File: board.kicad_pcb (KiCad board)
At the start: 2 copper layers, 40 parts, among them J1 TEMPS, J2 OLED, J3 RELAY, J4 RELAY_EN, J5 PWR_IN, J6 CONN_PROG, Q1 BC847, Q2 BC847, SW1 SW_RST, SW2 SW_RST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

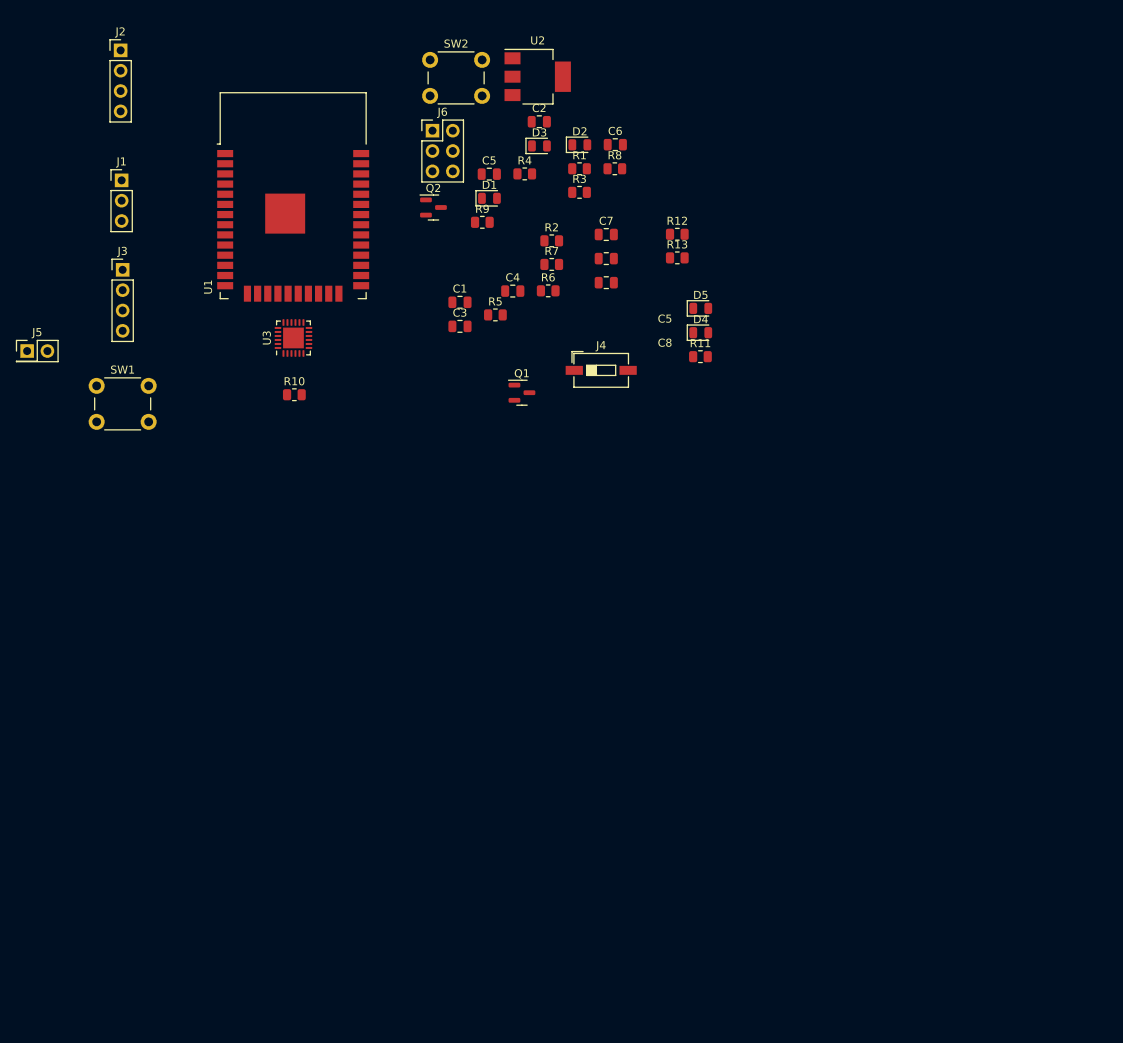
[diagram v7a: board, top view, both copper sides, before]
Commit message: feat: added relays and reworked programming
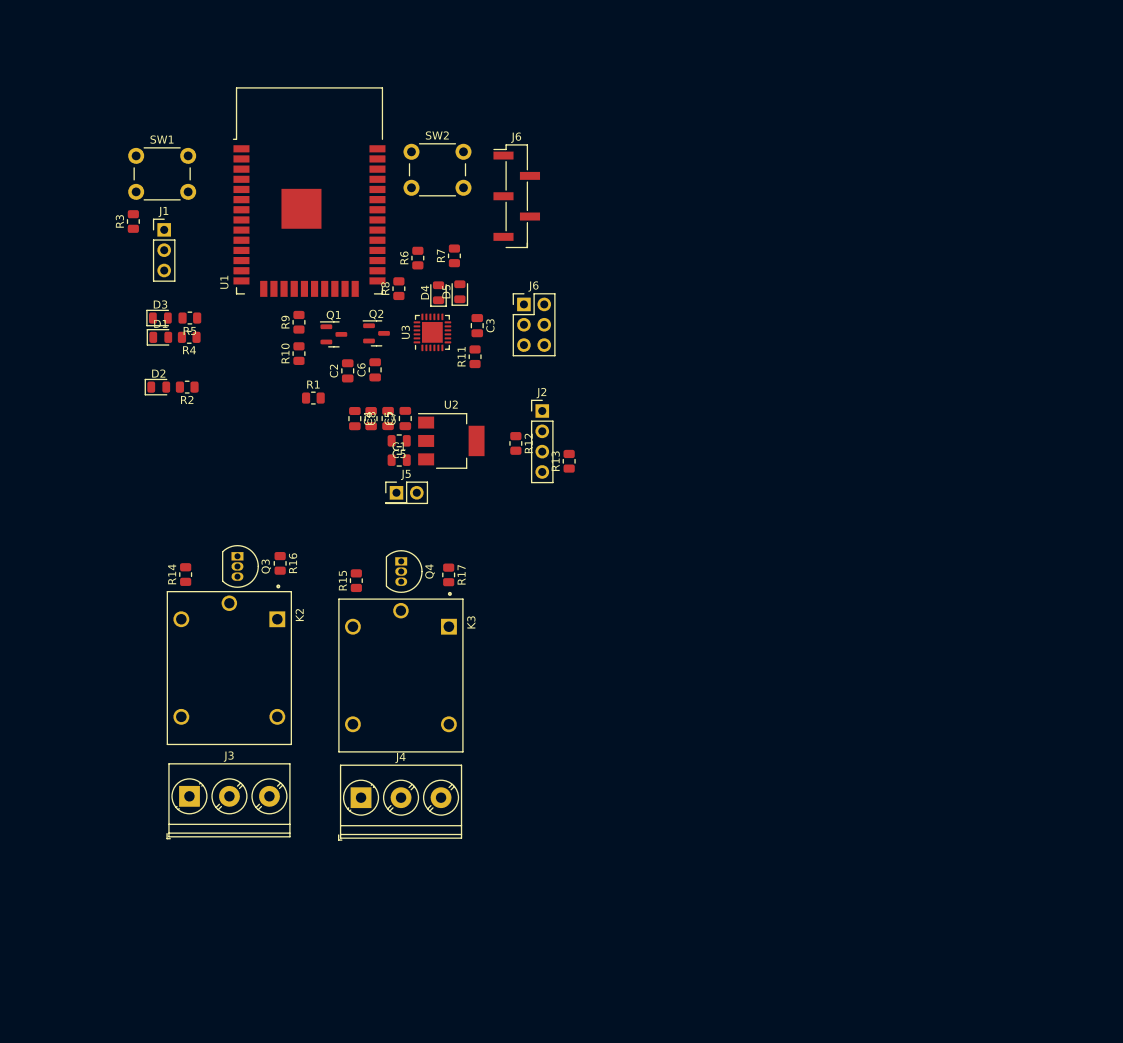
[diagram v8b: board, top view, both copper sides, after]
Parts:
- added J6: Conn_01x05_Female, Connector_PinHeader_2.54mm:PinHeader_1x05_P2.54mm_Vertical_SMD_Pin1Left, F.Cu at (90.7, 37.3)
- added K2: SRD-05VDC-SL-C, SRD-05VDC-SL-C:RELAY_SRD-05VDC-SL-C, F.Cu at (54.7, 96.3)
- added K3: SRD-05VDC-SL-C, SRD-05VDC-SL-C:RELAY_SRD-05VDC-SL-C, F.Cu at (76.2, 97.2)
- added Q3: BS170, Package_TO_SOT_THT:TO-92_Inline, F.Cu at (55.8, 82.3)
- added Q4: BS170, Package_TO_SOT_THT:TO-92_Inline, F.Cu at (76.2, 82.9)
- added R14: R, Resistor_SMD:R_0805_2012Metric, F.Cu at (49.3, 84.6)
- added R15: R, Resistor_SMD:R_0805_2012Metric, F.Cu at (70.6, 85.3)
- added R16: R, Resistor_SMD:R_0805_2012Metric, F.Cu at (61.1, 83.2)
- added R17: R, Resistor_SMD:R_0805_2012Metric, F.Cu at (82.2, 84.6)
- J3: value RELAY -> Screw_Terminal_01x03; footprint Connector_PinHeader_2.54mm:PinHeader_1x04_P2.54mm_Vertical -> TerminalBlock_Phoenix:TerminalBlock_Phoenix_PT-1,5-3-5.0-H_1x03_P5.00mm_Horizontal
- J4: value RELAY_EN -> Screw_Terminal_01x03; footprint Button_Switch_SMD:SW_DIP_SPSTx01_Slide_6.7x4.1mm_W6.73mm_P2.54mm_LowProfile_JPin -> TerminalBlock_Phoenix:TerminalBlock_Phoenix_PT-1,5-3-5.0-H_1x03_P5.00mm_Horizontal
- R2: value 1k -> 1k2
- R4, R5: value 330 -> 1k2
- moved J2 69.4 mm to (93.9, 64.1)
- moved J3 66.3 mm to (49.8, 112.3)
- moved J4 61.3 mm to (71.2, 112.5)
- moved D2 60.7 mm to (45.9, 61.1)
- moved R3 55.9 mm to (42.7, 40.4), turned to 90 degrees
- moved D3 52.0 mm to (46.1, 52.5)
- moved J5 49.5 mm to (75.6, 74.4)
- moved R2 49.1 mm to (49.5, 61.1), turned to 180 degrees
- moved U2 46.8 mm to (82.5, 67.9)
- moved R4 46.6 mm to (49.7, 54.9), turned to 180 degrees
- moved D1 44.6 mm to (46.2, 54.9)
- moved R1 43.9 mm to (65.2, 62.5)
- moved C6 41.1 mm to (73.0, 59.0), turned to 90 degrees
- moved C2 39.3 mm to (69.5, 59.1), turned to 90 degrees
- moved R5 38.2 mm to (49.8, 52.5), turned to 180 degrees
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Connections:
- J3 pad 1: GND -> Net-(J3-Pad1)
- J3 pad 2: CH1 -> Net-(J3-Pad2)
- J3 pad 3: CH2 -> Net-(J3-Pad3)
- J4 pad 1: /RELAY_V -> Net-(J4-Pad1)
- J4 pad 2: VBUS -> Net-(J4-Pad2)
